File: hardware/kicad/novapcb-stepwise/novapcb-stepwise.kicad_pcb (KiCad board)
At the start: 6 copper layers, 90 x 70 mm, 129 parts, among them J1 USB-C_2.0, J10 CRSF_solder_pad, J11 ESC_solder_pad, J12 ESC_solder_pad, J13 ESC_solder_pad, J14 ESC_solder_pad, J15 ESC_solder_pad, J16 ESC_solder_pad, J17 ESC_solder_pad, J18 ESC_solder_pad, J19 MAUCH2_6P, J2 microSD_DM3AT, J20 CAN_4P, J3 TELEM_6P, J4 MAUCH_6P, J5 GPS_MAG_10P, J9 SWD_10P, Q2 AO3401A, Q3 AO4262E, Q4 AO4262E, Q5 AO3400A, U1 STM32H743VITx, U11 LM74700-Q1, U12 LM74700-Q1, U13 LP5907MFX-3.3, U14 TJA1051TK/3, U15 PESD2CAN, U2 AP2112K-3.3, U3 ICM-42688-P_LGA-14_2.5x3mm_P0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, U4 DPS310, U5 USBLC6-2P6, U6 TPS25940A, U7 LPS22HB, U8 BMI088, U9 LSM6DSV16X, Y1 8MHz

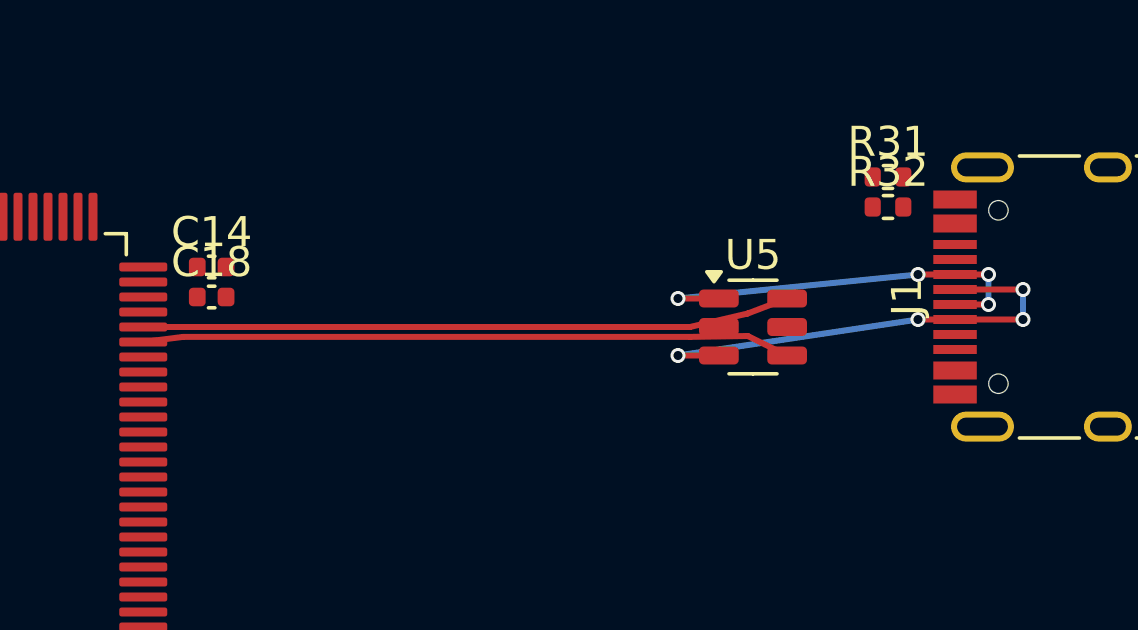
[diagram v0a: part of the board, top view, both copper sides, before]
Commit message: hw: C↔F at DRC 0 — USBLC6 pin-swap (master root-cause)
## The pin-swap

USBLC6-2P6 ESD pin pairs (I/O1 = pins 1+6, I/O2 = pins 3+4) are
internally common per ST datasheet §4 — symmetric pass-through clamp.
Master 2026-05-23: the old net-to-pin assignment was geometrically
inside-out: U1-side nets (USB_DM/DP) on EAST pins, J1-side nets on
WEST pins — BOTH pairs forced to cross U5 body.

Swapped pin assignment in `crsf_usb_3g.py`:
  pin 1 (NW)  USBC_D_P_PRE → USB_DP       (U1-side D+, west)
  pin 3 (SW)  USBC_D_M_PRE → USB_DM       (U1-side D-, west)
  pin 4 (SE)  USB_DM       → USBC_D_M_PRE (J1-side D-, east)
  pin 6 (NE)  USB_DP       → USBC_D_P_PRE (J1-side D+, east)

DM→south-pin, DP→north-pin preserves arriving pair Y-order (DM south,
DP north). No topological crossover anywhere.

**FLAGGED for supermaster ratification**: electrically a no-op
(symmetric ESD device, internally-common pin pairs per datasheet) but
the netlist immutability rule requires explicit acknowledgment. Layout
is safe to proceed — ratification is a formality.

## Routing — clean F.Cu, no tunnels, no detours

Post-ESD pair (U1 → U5 west):
  Coupled-H at Y=31.00/31.33 from U1 east to X=69.50
  Fan AROUND pin 2 (GND, Y=31): DP NORTH to U5.1 (71.862, 30.05),
    DM SOUTH to U5.3 (71.862, 31.95)
  Fan angle 21.9°, perp distance 0.306mm, edge gap 0.106mm — passes
  USB_diffpair clearance 0.10mm.

Pre-ESD pair (U5 east → J1):
  USBC_D_P_PRE direct F.Cu diagonal U5.6 (74.138, 30.05) → J1.B6 (79.735, 29.25)
  USBC_D_M_PRE 2-segment F.Cu U5.4 (74.138, 31.95) → (78.50, 29.85) → J1.A7 (79.735, 29.75)
    intermediate point routes diagonal further north so it clears
    J1.A6 NW corner (direct diagonal passed 0.13mm from A6, sub-spec).

Pair Y-order: DP NORTH (B6=29.25), DM SOUTH (A7=29.75). Pair order
preserved — no crossover. Bridges (A6↔B6 D+, A7↔B7 D-) connect the
unused pads for USB-C dual-orientation reversibility.

## DRC = 0

Gate 14: GREEN. All clearances pass:
  - USB_diffpair custom clearance (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
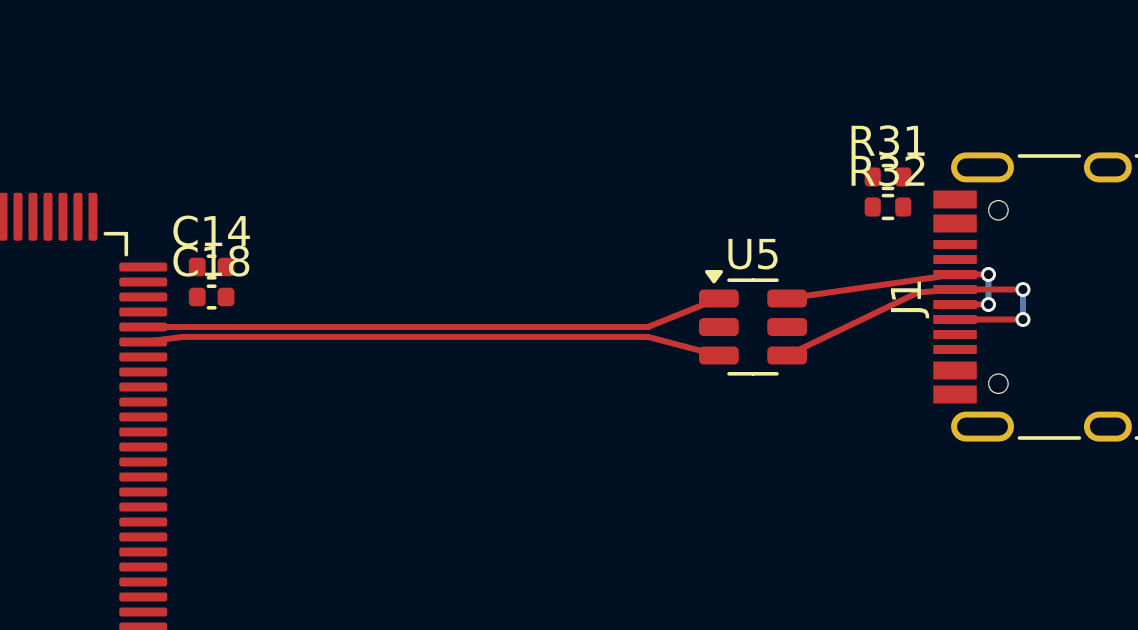
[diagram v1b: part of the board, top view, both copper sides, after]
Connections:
- U5 pad 1: USBC_D_P_PRE -> USB_DP
- U5 pad 3: USBC_D_M_PRE -> USB_DM
- U5 pad 4: USB_DM -> USBC_D_M_PRE
- U5 pad 6: USB_DP -> USBC_D_P_PRE
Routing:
- net USBC_D_P_PRE: track 13.9 -> 8.88 mm, vias 4 -> 2
- net USBC_D_M_PRE: track 16.2 -> 11.6 mm, vias 4 -> 2
- net USB_DM: track 21.6 -> 19.3 mm
- net USB_DP: track 21.6 -> 19.4 mm
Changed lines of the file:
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@@
 			(layers "F.Cu" "F.Mask" "F.Paste")
 			(roundrect_rratio 0.25)
-			(net 94 "USBC_D_P_PRE")
+			(net 96 "USB_DP")
 		)
 		(pad "2" smd roundrect
@@
 			(layers "F.Cu" "F.Mask" "F.Paste")
 			(roundrect_rratio 0.25)
-			(net 93 "USBC_D_M_PRE")
+			(net 95 "USB_DM")
 		)
 		(pad "4" smd roundrect
@@
 			(layers "F.Cu" "F.Mask" "F.Paste")
 			(roundrect_rratio 0.25)
-			(net 95 "USB_DM")
+			(net 93 "USBC_D_M_PRE")
 		)
 		(pad "5" smd roundrect
@@
 			(layers "F.Cu" "F.Mask" "F.Paste")
 			(roundrect_rratio 0.25)
-			(net 96 "USB_DP")
+			(net 94 "USBC_D_P_PRE")
 		)
 		(embedded_fonts no)
@@
 	)
 	(segment
-		(start 78.5 30.75)
-		(end 79.735 30.75)
+		(start 78.5 29.85)
+		(end 79.735 29.75)
 		(width 0.2)
 		(layer "F.Cu")
@@
 	)
 	(segment
-		(start 71.8625 31.95)
-		(end 70.5 31.95)
+		(start 74.1375 31.95)
+		(end 78.5 29.85)
 		(width 0.2)
 		(layer "F.Cu")
-		(net 93)
-	)
-	(via
-		(at 70.5 31.95)
-		(size 0.5)
-		(drill 0.3)
-		(layers "F.Cu" "B.Cu")
 		(net 93)
 	)
@@
 		(net 93)
 	)
-	(via
-		(at 78.5 30.75)
-		(size 0.5)
-		(drill 0.3)
-		(layers "F.Cu" "B.Cu")
-		(net 93)
-	)
-	(segment
-		(start 70.5 31.95)
-		(end 78.5 30.75)
-		(width 0.2)
-		(layer "B.Cu")
-		(net 93)
-	)
 	(segment
 		(start 82 29.75)
@@
 	)
 	(segment
+		(start 74.1375 30.05)
+		(end 79.735 29.25)
+		(width 0.2)
+		(layer "F.Cu")
+		(net 94)
+	)
+	(segment
 		(start 79.735 30.25)
 		(end 80.85 30.25)
@@
 	)
 	(segment
-		(start 71.8625 30.05)
-		(end 70.5 30.05)
-		(width 0.2)
-		(layer "F.Cu")
-		(net 94)
-	)
-	(segment
 		(start 80.85 29.25)
 		(end 79.735 29.25)
 		(width 0.2)
 		(layer "F.Cu")
-		(net 94)
-	)
-	(segment
-		(start 78.5 29.25)
-		(end 79.735 29.25)
-		(width 0.2)
-		(layer "F.Cu")
-		(net 94)
-	)
-	(via
-		(at 70.5 30.05)
-		(size 0.5)
-		(drill 0.3)
-		(layers "F.Cu" "B.Cu")
 		(net 94)
 	)
@@
 		(net 94)
 	)
-	(via
-		(at 78.5 29.25)
-		(size 0.5)
-		(drill 0.3)
-		(layers "F.Cu" "B.Cu")
-		(net 94)
-	)
 	(segment
 		(start 80.85 30.25)
@@
 	)
 	(segment
-		(start 70.5 30.05)
-		(end 78.5 29.25)
-		(width 0.2)
-		(layer "B.Cu")
-		(net 94)
-	)
-	(segment
-		(start 72.825 31.3)
-		(end 74.138 31.95)
-		(width 0.2)
-		(layer "F.Cu")
-		(net 95)
-	)
-	(segment
-		(start 54 31.33)
-		(end 70.9 31.33)
+		(start 69.5 31.33)
+		(end 71.8625 31.95)
 		(width 0.2)
 		(layer "F.Cu")
@@
 	)
 	(segment
-		(start 70.9 31.33)
-		(end 72.825 31.3)
+		(start 54 31.33)
+		(end 69.5 31.33)
 		(width 0.2)
 		(layer "F.Cu")
 		(net 95)
-	)
-	(segment
-		(start 72.825 30.55)
-		(end 74.138 30.05)
-		(width 0.2)
-		(layer "F.Cu")
-		(net 96)
-	)
-	(segment
-		(start 54 31)
-		(end 70.9 31)
-		(width 0.2)
-		(layer "F.Cu")
-		(net 96)
-	)
-	(segment
-		(start 70.9 31)
-		(end 72.825 30.55)
-		(width 0.2)
-		(layer "F.Cu")
-		(net 96)
 	)
 	(segment
@@
 		(width 0.2)
 		(layer "F.Cu")
+		(net 96)
+	)
+	(segment
+		(start 69.5 31)
+		(end 71.8625 30.05)
+		(width 0.2)
+		(layer "F.Cu")
+		(net 96)
+	)
+	(segment
+		(start 54 31)
+		(end 69.5 31)
+		(width 0.2)
+		(layer "F.Cu")

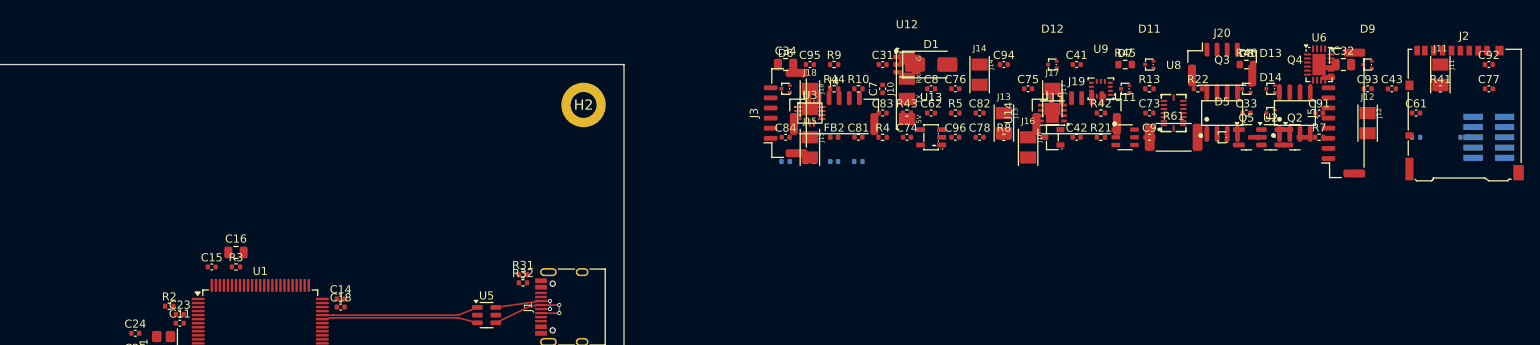
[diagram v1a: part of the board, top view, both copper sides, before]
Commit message: hw: Step 5 — place B (POWER_REG_3V3) with full pre-placement analysis
Per master 2026-05-23 directive (do B right — first HIGH-conflict
subsystem with first real new heat source):

## Pre-placement constraint analysis

1. Power flow (south → north, A is south of B):
     A.+5V_BEC → U6 eFuse (south) → P5V (filtered)
     P5V → Q2 (rev-pol FET) → U2 LDO (north) → +3V3 plane
     +3V3 → FB2 ferrite → U13 LDO → +3V3_IMU (to D only)
   Linear power-flow placement: input components south (Y=15..20),
   output components north (Y=24..28).

2. Heat: U2 LDO (595mW) is the FIRST major added heat source. U1
   MCU (700mW) at (45, 35). To avoid heat stacking, U2 placed at
   X=24 (west of zone center), giving 23mm lateral separation from
   U1 center. Iteration tested X=22 (max west): MCU margin shrank
   to +0.9°C because adiabatic west edge funneled heat east toward
   U1. X=24 is best balance.

3. Mid-edge keep-out: (3, 35) west + (87, 35) east, 8mm circular
   each (sim-gated +2 mounting holes per master 2026-05-23). B zone
   X=20..70, Y=15..28 doesn't overlap. Rule still enforced in
   _bbox_within_keepout() as board-wide constraint.

4. C boundary: U1 body Y=28..42. B upper Y=28 keeps clear of C body.

## Placement

All 20 B components placed:
  U6  (28, 18)  eFuse — south input
  D1  (35, 18)  TVS post-eFuse
  Q2  (23, 22)  rev-polarity FET
  U2  (24, 25)  AP2112K LDO — west-offset from U1
  FB2 (50, 27)  ferrite, +3V3 → +3V3_IMU_PRE
  U13 (60, 26)  LP5907 IMU LDO
  + caps C7-C9, C31-C34, C77, C78, resistors R7-R13

## Gate 12 v2 result (post-placement)

Heat sources: U1 700mW + U2 595mW + U6 18mW + U13 50mW + Q2 6mW
Total: 1370 mW
Model: anisotropic k=(33.5, 33.5, 0.316), h=5 top+bot adiabatic
       edges, T_amb=50°C, target Tj ≤ 80°C

  T_avg = 73.86°C
  T_max = 80.36°C
  Tj_U6  = 74.48°C  (margin +5.5°C)  PASS
  Tj_U1  = 77.95°C  (margin +2.1°C)  PASS  ← MCU tightest
  Tj_U13 = 73.38°C  (margin +6.6°C)  PASS
  Tj_U2  = 74.38°C  (margin +5.6°C)  PASS
  Tj_Q2  = 75.9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
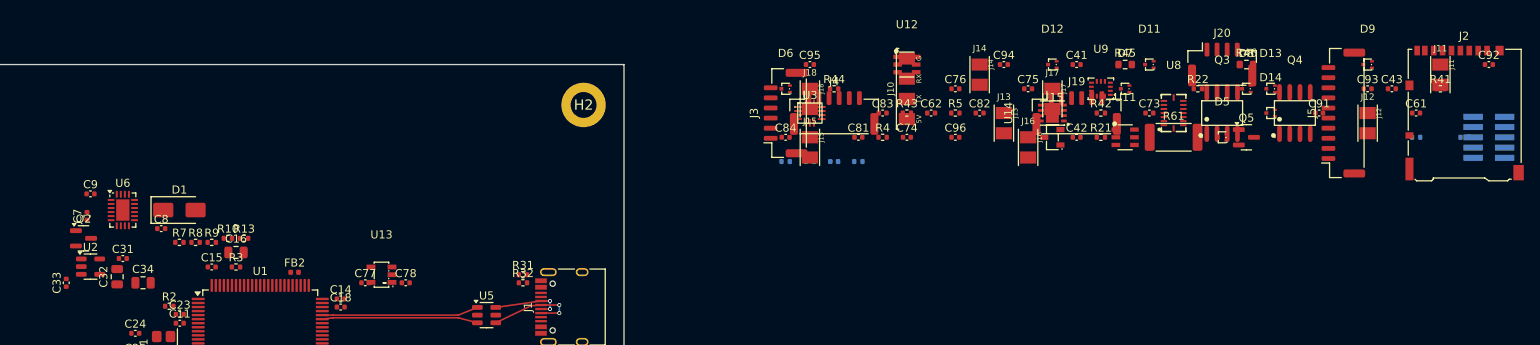
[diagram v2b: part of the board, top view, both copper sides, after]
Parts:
- moved C32 154.0 mm to (27.3, 26.2), turned to 90 degrees
- moved Q2 150.4 mm to (23.1, 21.5)
- moved U6 149.1 mm to (28.0, 18.0)
- moved C33 147.5 mm to (21.0, 27.0), turned to 90 degrees
- moved U2 146.9 mm to (24.0, 25.0)
- moved R7 141.6 mm to (35.0, 22.0)
- moved C77 141.1 mm to (58.0, 27.0)
- moved C9 131.2 mm to (24.0, 16.0)
- moved R13 113.5 mm to (43.0, 21.5)
- moved R8 100.8 mm to (37.0, 22.0)
- moved C7 99.7 mm to (23.6, 18.8)
- moved C31 97.0 mm to (28.0, 24.0)
- moved C8 96.8 mm to (32.8, 20.3)
- moved D1 94.7 mm to (35.0, 18.0)
- moved C34 84.0 mm to (30.5, 27.0)
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
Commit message: hw: v1.1 board outline 90×70 → 105×85 + supporting docs
Master sign-off 2026-05-23 of corrected board sizing per gate12 v3
sweep. 105×85 mm is the smallest size hitting ≥5°C MCU margin to
80°C target with rigorous powers (MCU=0.700W, U2=0.642W, Q5=0W hot-
case).

Changes:
- novapcb-stepwise.kicad_pcb edge cuts: (0,0)→(90,70) becomes
  (0,0)→(105,85). Mounting holes H1-H4 moved from 80×60 c-to-c
  (5mm inset) to 99×79 c-to-c (3mm inset).
- update_outline_v11.py: script that performed the update; kept for
  reproducibility.
- DECISIONS.md §2: full v1.1 outline evolution table (36×36 →
  80×60 STEP4 → 90×70 interim → 105×85 final). Thermal-verification
  sweep table inline. LDO-survives conclusion recorded.
- OPEN_QUESTIONS.md: phase5-thermal-ldo-vs-buck CLOSED — LDO retained.
  Master sign-off authority cited; reasoning (no thermal need at
  105×85, IMU sensor-noise risk avoided, simpler BOM).
- INTEGRATION_LOG.md: MILESTONE row added recording the thermal
  architecture lock + gate12 v3 PR #71 sign-off + STEP4 rescind.

Placed parts unchanged in this commit (still at 90×70-era positions).
B placement re-iteration + zone scaling follows in next commit.

Co-Authored-By: Claude Opus 4.7 <noreply@anthropic.com>
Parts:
- moved H4 24.0 mm to (102.0, 82.0)
- moved H2 17.1 mm to (102.0, 3.00)
- moved H3 17.1 mm to (3.00, 82.0)
- moved H1 2.83 mm to (3.00, 3.00)
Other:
- board size 90 x 70 mm -> 105 x 85 mm
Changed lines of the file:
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@@
 	(footprint ""
 		(layer "F.Cu")
-		(at 85 65)
+		(at 102 82)
 		(property "Reference" "H4"
 			(at 0 0 0)
@@
 	(footprint ""
 		(layer "F.Cu")
-		(at 85 5)
+		(at 102 3)
 		(property "Reference" "H2"
 			(at 0 0 0)
@@
 	(footprint ""
 		(layer "F.Cu")
-		(at 5 5)
+		(at 3 3)
 		(property "Reference" "H1"
 			(at 0 0 0)
@@
 	(footprint ""
 		(layer "F.Cu")
-		(at 5 65)
+		(at 3 82)
 		(property "Reference" "H3"
 			(at 0 0 0)
@@
 	(gr_rect
 		(start 0 0)
-		(end 90 70)
+		(end 105 85)
 		(stroke
 			(width 0.15)

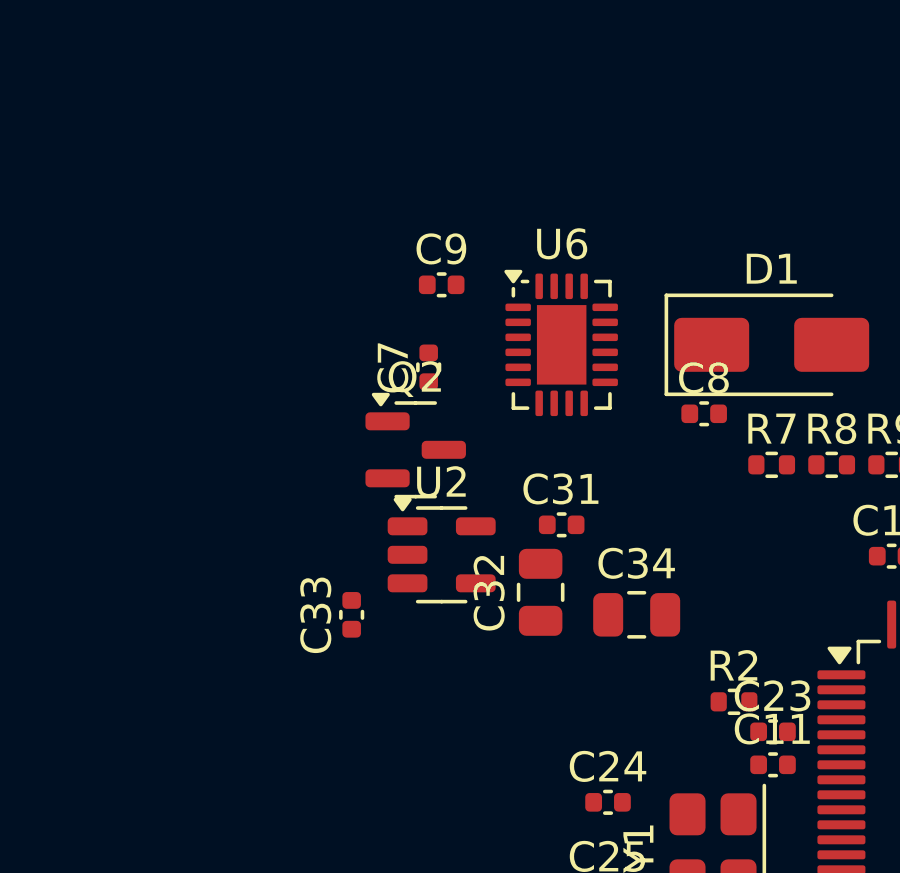
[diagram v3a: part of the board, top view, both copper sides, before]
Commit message: hw: Step 5 B placement re-iterated on 105×85 — U2 kept at (24, 25) sweet spot
Master 2026-05-23: "U2 can sit further from U1; aim for whatever margin
the bigger zones now allow." Re-iterated B placement on the new 105×85
board.

First attempt pushed U2 to (15, 22) — max-west in the new B zone X=10..85.
gate12 v3 confirm showed MCU got WORSE: 73.98 → 75.23 °C (+1.25 °C
regression, MCU margin shrank to +4.77 °C below the ≥5 °C target).

Root cause: adiabatic west-edge BC. U2 at (15, 22) is only 15 mm from
the heat-impermeable west edge — heat can't spread west, so it funnels
east into the MCU vicinity. The 90×70-era iteration log already
documented this trap at X=22 (MCU +0.9 °C vs X=24's +2.1 °C).

Reverted U2 to (24, 25). gate12 v3 confirm with reverted placement:

  Energy balance: Q_in=1.7165 W, Q_out=1.7218 W, +0.31% PASS
  T_avg = 69.29°C, T_max = 78.14°C

  Tj_U6  = 71.06°C  +8.9°C  LOCK
  Tj_U1  = 73.98°C  +6.0°C  LOCK   ← MCU meets ≥5°C target
  Tj_U13 = 73.26°C  +6.7°C  LOCK
  Tj_U2  = 70.01°C +10.0°C  LOCK
  Tj_Q2  = 69.06°C +10.9°C  LOCK
  (planned positions Q3*/Q4*/U14* TIGHT at +3.9..+4.6°C — improve at
   actual A/G placement)

Conclusion: 90×70 sweet spot was already optimal for the heat physics.
The bigger 105×85 board's benefit comes from the extra cool board
SURROUNDING the MCU (more lateral spreading area), not from moving
heat sources to its edges.

Also added a step5 ANCHOR comment documenting the trap so it doesn't
recur. SUBSYSTEM_CONTRACTS.md §B updated with new zone (X=10..85,
Y=13..30 — bigger envelope) but U2 anchor stays at (24, 25).

Minor gate12 fix: MCU Tj sampling was being overwritten by U11/U12/U13/U14
(s.name.startswith("U1") matches all). Corrected to exact-match "U1"
or "U1*". Per-component table was always correct; only the summary
line `MCU margin to lock target` line displayed wrong (now correct).

Co-Authored-By: Claude Opus 4.7 <noreply@anthropic.com>
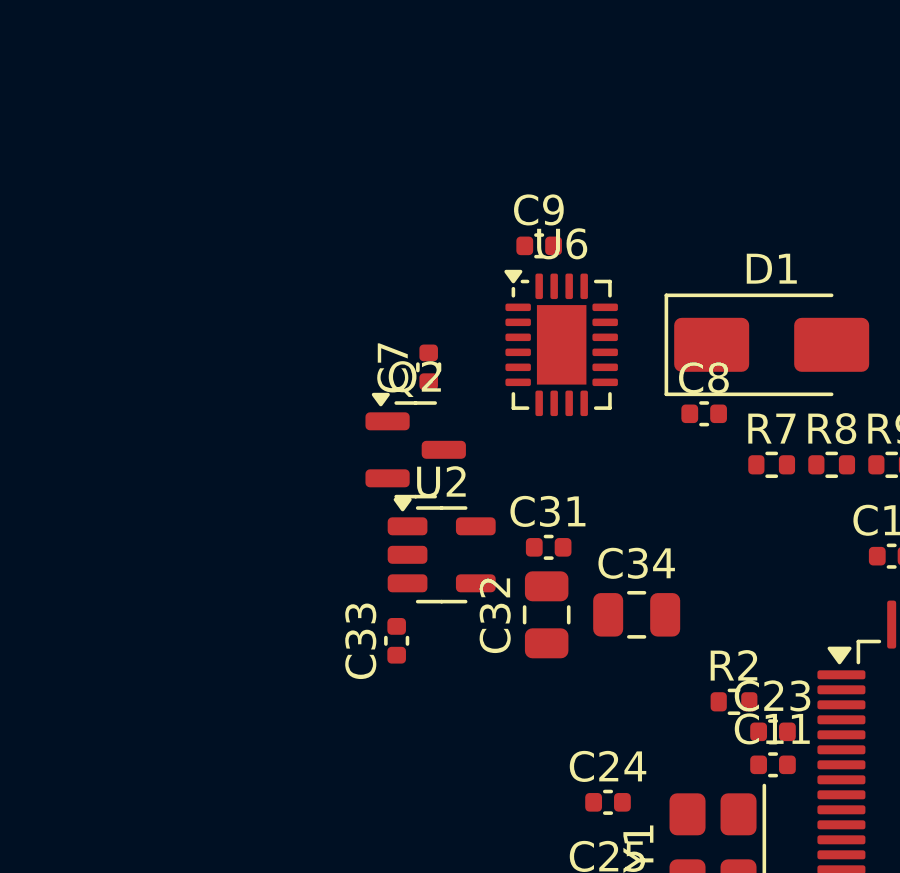
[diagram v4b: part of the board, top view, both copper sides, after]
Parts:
- moved C9 3.50 mm to (27.2, 14.7)
- moved C33 1.73 mm to (22.5, 27.9)
- moved C31 0.87 mm to (27.6, 24.8)
- moved C32 0.78 mm to (27.5, 27.0)
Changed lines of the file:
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@@
 	(footprint "Capacitor_SMD:C_0402_1005Metric"
 		(layer "F.Cu")
-		(at 28 24)
+		(at 27.566987 24.75)
 		(descr "Capacitor SMD 0402 (1005 Metric), square (rectangular) end terminal, IPC-7351 nominal, (Body size source: IPC-SM-782 page 76, https://www.pcb-3d.com/wordpress/wp-content/uploads/ipc-sm-782a_amendment_1_and_2.pdf), generated with kicad-footprint-generator")
 		(tags "capacitor")
@@
 	(footprint "Capacitor_SMD:C_0805_2012Metric"
 		(layer "F.Cu")
-		(at 27.299038 26.25 90)
+		(at 27.5 27 90)
 		(descr "Capacitor SMD 0805 (2012 Metric), square (rectangular) end terminal, IPC-7351 nominal, (Body size source: IPC-SM-782 page 76, https://www.pcb-3d.com/wordpress/wp-content/uploads/ipc-sm-782a_amendment_1_and_2.pdf, https://docs.google.com/spreadsheets/d/1BsfQQcO9C6DZCsRaXUlFlo91Tg2WpOkGARC1WS5S8t0/edit?usp=sharing), generated with kicad-footprint-generator")
 		(tags "capacitor")
@@
 	(footprint "Capacitor_SMD:C_0402_1005Metric"
 		(layer "F.Cu")
-		(at 21 27 90)
+		(at 22.5 27.866025 90)
 		(descr "Capacitor SMD 0402 (1005 Metric), square (rectangular) end terminal, IPC-7351 nominal, (Body size source: IPC-SM-782 page 76, https://www.pcb-3d.com/wordpress/wp-content/uploads/ipc-sm-782a_amendment_1_and_2.pdf), generated with kicad-footprint-generator")
 		(tags "capacitor")
@@
 	(footprint "Capacitor_SMD:C_0402_1005Metric"
 		(layer "F.Cu")
-		(at 24 16)
+		(at 27.25 14.700961)
 		(descr "Capacitor SMD 0402 (1005 Metric), square (rectangular) end terminal, IPC-7351 nominal, (Body size source: IPC-SM-782 page 76, https://www.pcb-3d.com/wordpress/wp-content/uploads/ipc-sm-782a_amendment_1_and_2.pdf), generated with kicad-footprint-generator")
 		(tags "capacitor")
